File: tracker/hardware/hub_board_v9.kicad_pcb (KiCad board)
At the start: 4 copper layers, 103 x 103 mm, 39 parts, among them U1 ESP32-S3-WROOM-1U-N8R8, U2 LoRa2021F33-2G4, U3 LoRa2021_Castellated, U4 SX1280, U5 MAX-M10S, U6 MS5611-01BA, U7 TPS7A02

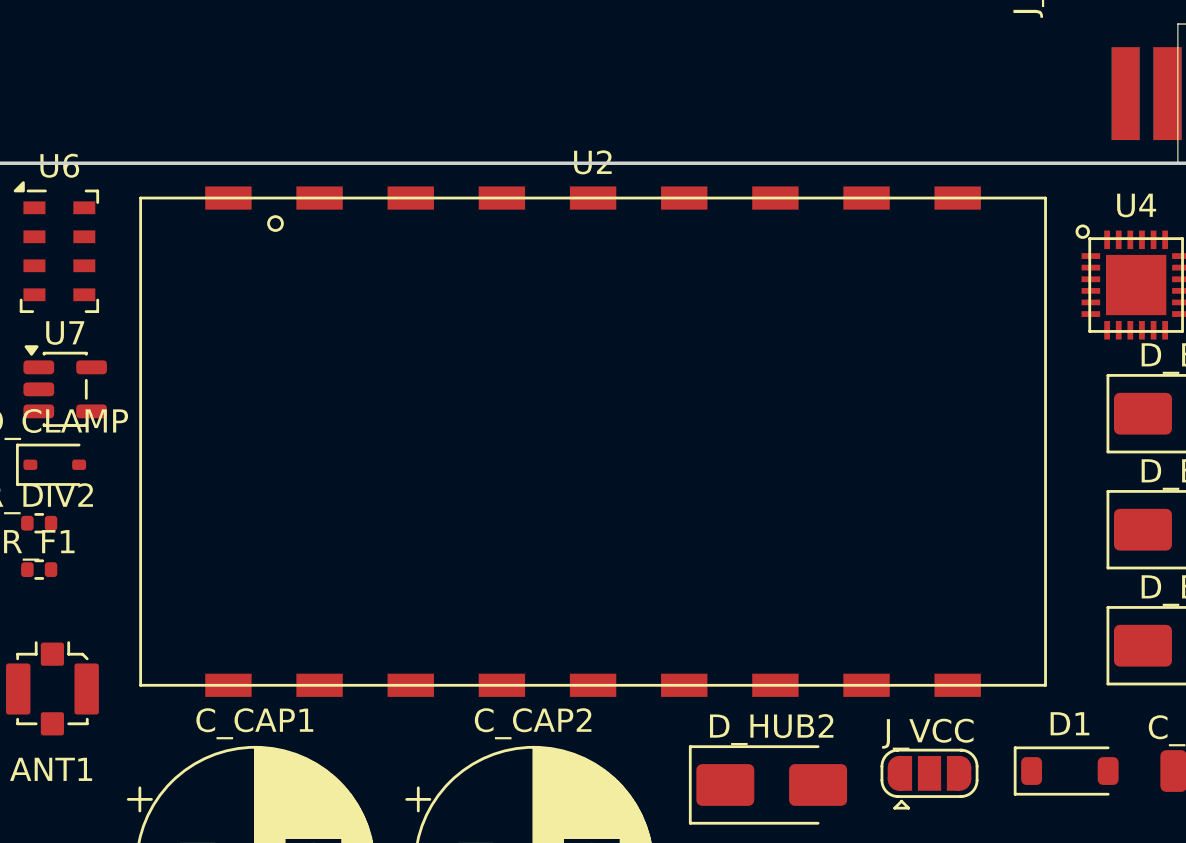
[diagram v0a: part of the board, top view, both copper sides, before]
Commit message: fix(hw/f33): derive the castellation land size from the operator-supplied 0.80mm datum
The F33 land pattern's pad POSITIONS were already verified against the vendor's own
Altium pad file; the pad SIZE was the one declared guess (2.0 x 1.0 mm, TODO(unverified)).
The operator read the vendor drawing (datasheet s9 "Mechanism Dimension" p8, an embedded
JPEG raster with no text layer, hence never extractable in-repo) and reported the
castellation hole diameter D = 0.80 +/- 0.10 mm.  That is the authoritative datum.

DERIVE the land instead of hard-coding it:
  rule: land = the castellation aperture grown by a uniform 0.25mm solder-fillet margin
        on every side.
    x (along the edge): D + 2*0.25 = 1.30mm  (was 2.0mm = 2.5xD);
                        gap to the next land = 3.9289 - 1.30 = 2.6289mm
    y (across the edge): D + 2*0.25 = 1.30mm, symmetric about the pad centre, which the
                        vendor file pins on the module edge and which must NOT move:
                          inward 0.65mm >= D/2 = 0.40mm
                          outward 0.65mm >= inward 0.65mm -- the hand-solder iron's
                          access is the design driver (every joint on this vehicle is
                          hand-soldered); 0.65mm clears a 0.5mm chisel tip.

- scripts/gen_f33_landpattern.py: the hard-coded LAND_*_MM constants are replaced by the
  derivation (CASTELLATION_D_MM, CASTELLATION_D_TOL_MM, LAND_FILLET_MARGIN_MM); the rule
  and arithmetic are in the docstring; the datum and its +/-0.1 tolerance are recorded;
  --land-length/--land-width are kept as explicit overrides; the TODO(unverified)
  land-size flag is DROPPED (no other TODO touched).
- All four committed footprint copies and the v9 design-of-record footprint regenerated.
  Pad POSITIONS unchanged: the 18 pad-centre list is byte-identical (sha256 960877b2...)
  before and after, the bbox is still 31.4312 x 21.0000mm, and only the pad-size histogram
  moves 2x1 -> 1.3x1.3.  --verify-all exits 0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
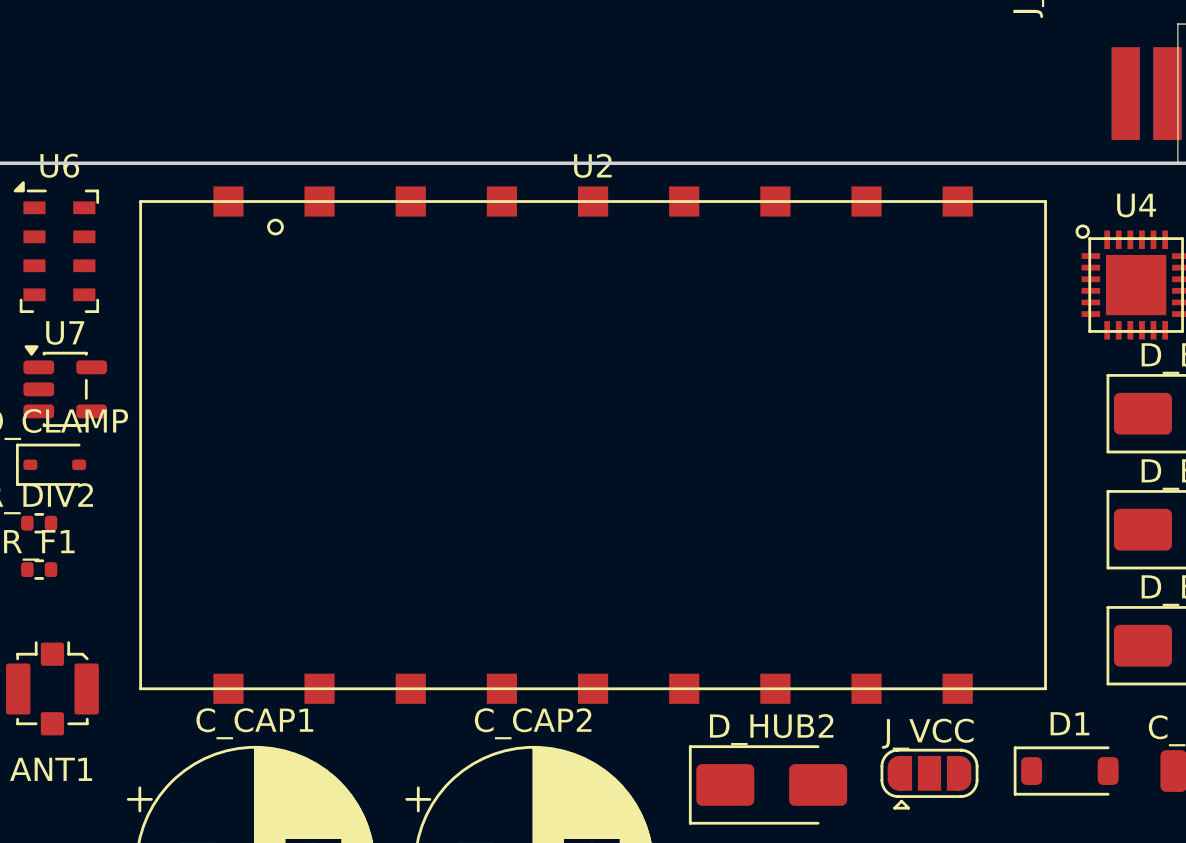
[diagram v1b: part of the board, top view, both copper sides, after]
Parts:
- moved U2 0.15 mm to (25.8, 12.2)
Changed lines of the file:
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@@
 	(footprint "balloon_flight_v9:LoRa2021F33_2G4"
 		(layer "F.Cu")
-		(at 25.845 12)
-		(descr "NiceRF LoRa2021F33-2G4, 18-pin castellated module (LR2021 + 2W PA + TCXO), 39x21mm. Pad CENTRES decoded from the vendor land file LORA2021F33-2G4 footprint_pads.pcb (pitch 3.9289mm, 9 pads on each 39mm edge). Land size 2.0x1.0 mm TODO(unverified): datasheet s9 p8 is a raster with no text layer.")
+		(at 25.845 12.15)
+		(descr "NiceRF LoRa2021F33-2G4, 18-pin castellated module (LR2021 + 2W PA + TCXO), 39x21mm. Pad CENTRES decoded from the vendor land file LORA2021F33-2G4 footprint_pads.pcb (pitch 3.9289mm, 9 pads on each 39mm edge). Land size 1.3 x 1.3 mm DERIVED from the operator-supplied castellation hole diameter D = 0.8 +/- 0.1 mm grown by a uniform 0.25 mm solder-fillet margin on every side (datasheet s9 p8, read by the operator 2026-10-07).")
 		(tags "LoRa LR2021 NiceRF F33 castellated PA 2W vendor-land-pattern")
 		(property "Reference" "U2"
@@
 		(pad "1" smd rect
 			(at -11.7867 -10.5)
-			(size 2 1)
+			(size 1.3 1.3)
 			(layers "F.Cu" "F.Mask" "F.Paste")
 			(net 17 "/F33_VCC")
@@
 		(pad "2" smd rect
 			(at -7.8578 -10.5)
-			(size 2 1)
+			(size 1.3 1.3)
 			(layers "F.Cu" "F.Mask" "F.Paste")
 			(net 51 "GND")
@@
 		(pad "3" smd rect
 			(at -3.9289 -10.5)
-			(size 2 1)
+			(size 1.3 1.3)
 			(layers "F.Cu" "F.Mask" "F.Paste")
 			(net 51 "GND")
@@
 		(pad "4" smd rect
 			(at 0 -10.5)
-			(size 2 1)
+			(size 1.3 1.3)
 			(layers "F.Cu" "F.Mask" "F.Paste")
 			(net 51 "GND")
@@
 		(pad "5" smd rect
 			(at 3.9289 -10.5)
-			(size 2 1)
+			(size 1.3 1.3)
 			(layers "F.Cu" "F.Mask" "F.Paste")
 			(net 1 "+3V3")
@@
 		(pad "6" smd rect
 			(at 7.8578 -10.5)
-			(size 2 1)
+			(size 1.3 1.3)
 			(layers "F.Cu" "F.Mask" "F.Paste")
 			(net 51 "GND")
@@
 		(pad "7" smd rect
 			(at 11.7867 -10.5)
-			(size 2 1)
+			(size 1.3 1.3)
 			(layers "F.Cu" "F.Mask" "F.Paste")
 			(net 51 "GND")
@@
 		(pad "8" smd rect
 			(at 15.7156 -10.5)
-			(size 2 1)
+			(size 1.3 1.3)
 			(layers "F.Cu" "F.Mask" "F.Paste")
 			(net 51 "GND")
@@
 		(pad "9" smd rect
 			(at 15.7156 10.5)
-			(size 2 1)
+			(size 1.3 1.3)
 			(layers "F.Cu" "F.Mask" "F.Paste")
 			(net 2 "/ANT1_433_TX")
@@
 		(pad "10" smd rect
 			(at 11.7867 10.5)
-			(size 2 1)
+			(size 1.3 1.3)
 			(layers "F.Cu" "F.Mask" "F.Paste")
 		)
 		(pad "11" smd rect
 			(at 7.8578 10.5)
-			(size 2 1)
+			(size 1.3 1.3)
 			(layers "F.Cu" "F.Mask" "F.Paste")
 			(net 51 "GND")
@@
 		(pad "12" smd rect
 			(at 3.9289 10.5)
-			(size 2 1)
+			(size 1.3 1.3)
 			(layers "F.Cu" "F.Mask" "F.Paste")
 			(net 16 "/F33_SCK")
@@
 		(pad "13" smd rect
 			(at 0 10.5)
-			(size 2 1)
+			(size 1.3 1.3)
 			(layers "F.Cu" "F.Mask" "F.Paste")
 			(net 11 "/F33_CS_N")
@@
 		(pad "14" smd rect
 			(at -3.9289 10.5)
-			(size 2 1)
+			(size 1.3 1.3)
 			(layers "F.Cu" "F.Mask" "F.Paste")
 			(net 10 "/F33_BUSY")
@@
 		(pad "15" smd rect
 			(at -7.8578 10.5)
-			(size 2 1)
+			(size 1.3 1.3)
 			(layers "F.Cu" "F.Mask" "F.Paste")
 			(net 14 "/F33_MOSI")
@@
 		(pad "16" smd rect
 			(at -11.7867 10.5)
-			(size 2 1)
+			(size 1.3 1.3)
 			(layers "F.Cu" "F.Mask" "F.Paste")
 			(net 13 "/F33_MISO")
@@
 		(pad "17" smd rect
 			(at -15.7156 10.5)
-			(size 2 1)
+			(size 1.3 1.3)
 			(layers "F.Cu" "F.Mask" "F.Paste")
 			(net 15 "/F33_RESET_N")
@@
 		(pad "18" smd rect
 			(at -15.7156 -10.5)
-			(size 2 1)
+			(size 1.3 1.3)
 			(layers "F.Cu" "F.Mask" "F.Paste")
 			(net 12 "/F33_IRQ")

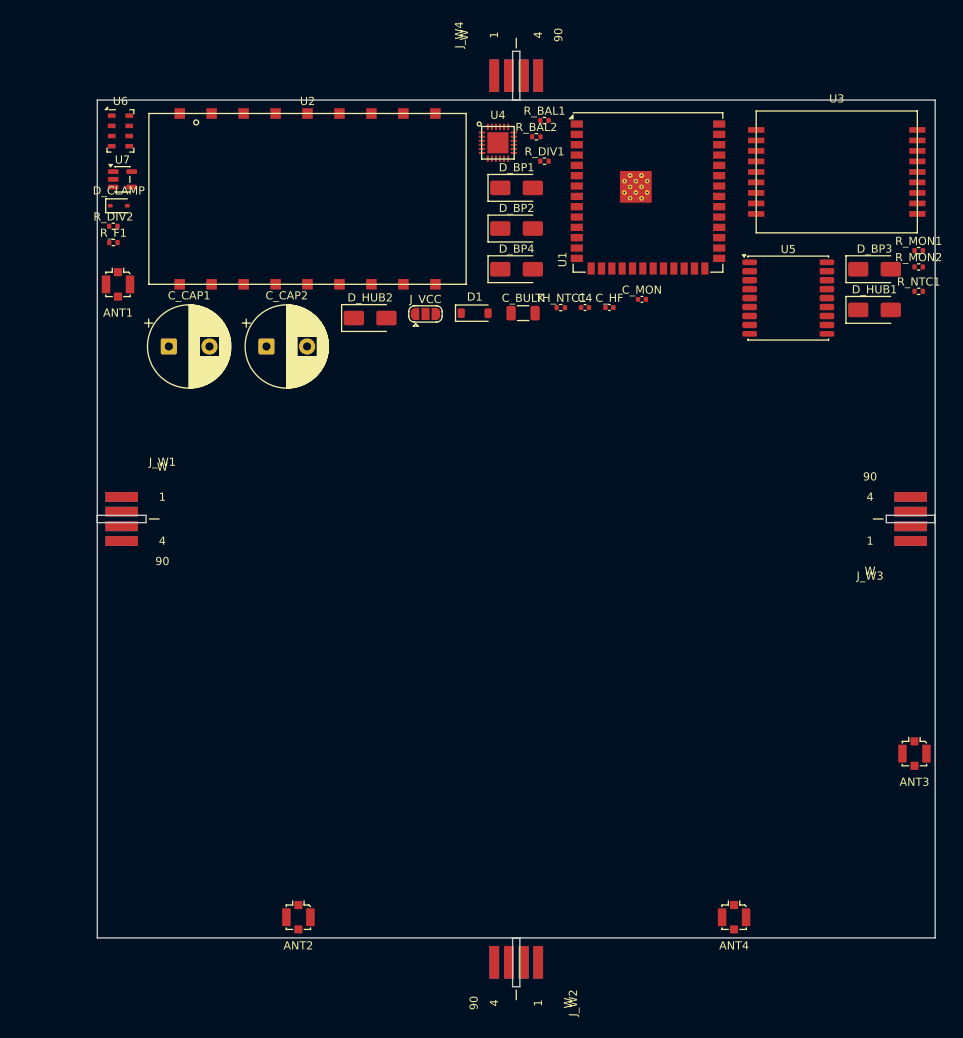
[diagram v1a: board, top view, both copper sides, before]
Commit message: fix(hw/hub): render fidelity — cells on the sun-facing face, faceted dark cells, no box parts
Recovered from a worker that timed out at 3600 s having completed the work but
not committed it. The generator died ONE LINE from publishing on:

    NameError: name 'KICAD9_3DMODEL_DIR' is not defined

because `${KICAD9_3DMODEL_DIR}` is a KiCad VARIABLE, not a Python name: inside
an f-string it parses as the expression KICAD9_3DMODEL_DIR. The module already
had a KICAD9_VAR constant for exactly this; the print did not use it. Fixed.

Three render defects, all verified after regeneration:

1. CELLS ON THE WRONG FACE (operator-reported, ADR-055 D6).
   PVA1/PVA2 were on B.Cu; every other footprint is F.Cu. ADR-055 D6 says the
   hub cells go on the UPPER/sun-facing face, and with a horizontal hub the
   downward face receives no direct sun. Now F.Cu.

2. CELLS RENDERED AS FLAT GREY SLABS (operator-reported).
   The hub cell model was a bare `Box` with ONE material (light grey), while the
   wing's was an `IndexedFaceSet` with TWO (dark cell face + light frame). That
   is why the wing's panels read as cells and the hub's as slabs. Now faceted
   with the dark 0.09 0.1 0.42 cell face, matching the wing.

3. IMPLAUSIBLY THICK PARTS (operator-reported).
   See the coverage report for every model's Z and its source.

Model split after regeneration: 25 library + 16 repo-local, unmapped: [].
Library models are referenced via ${KICAD9_3DMODEL_DIR}, so a render now
REQUIRES: export KICAD9_3DMODEL_DIR=/usr/share/kicad/3dmodels

Board sha256 1d4e9509e9528f5b5b696f7a52b644518c5bc5070fe633526a0085ee2df7f259
Full-duty check still reports honestly: 4 x LARGE = 122.2 cm2 > plate 106.09 cm2,
so the 4-cell 106.1 cm2 configuration is NOT placeable on a 103 x 103 mm plate
(the packing problem the operator's overhang decision resolves).
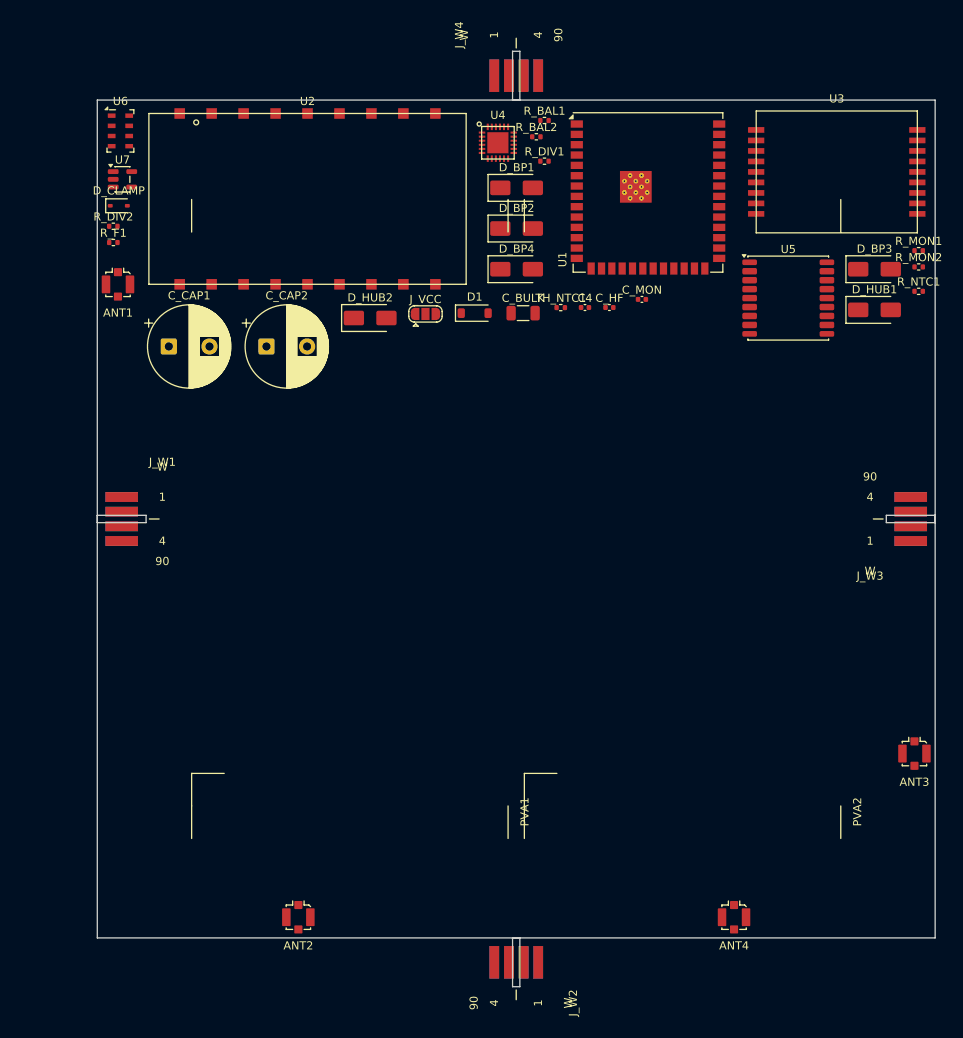
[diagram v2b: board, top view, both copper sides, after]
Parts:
- added PVA1: SolarCell_78x39mm, Array_Cells:SolarCell_LARGE_78x39mm, F.Cu at (31.1, 51.5)
- added PVA2: SolarCell_78x39mm, Array_Cells:SolarCell_LARGE_78x39mm, F.Cu at (72.0, 51.5)

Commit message: feat(hw/hub): implement ADR-063 overhanging solar carrier
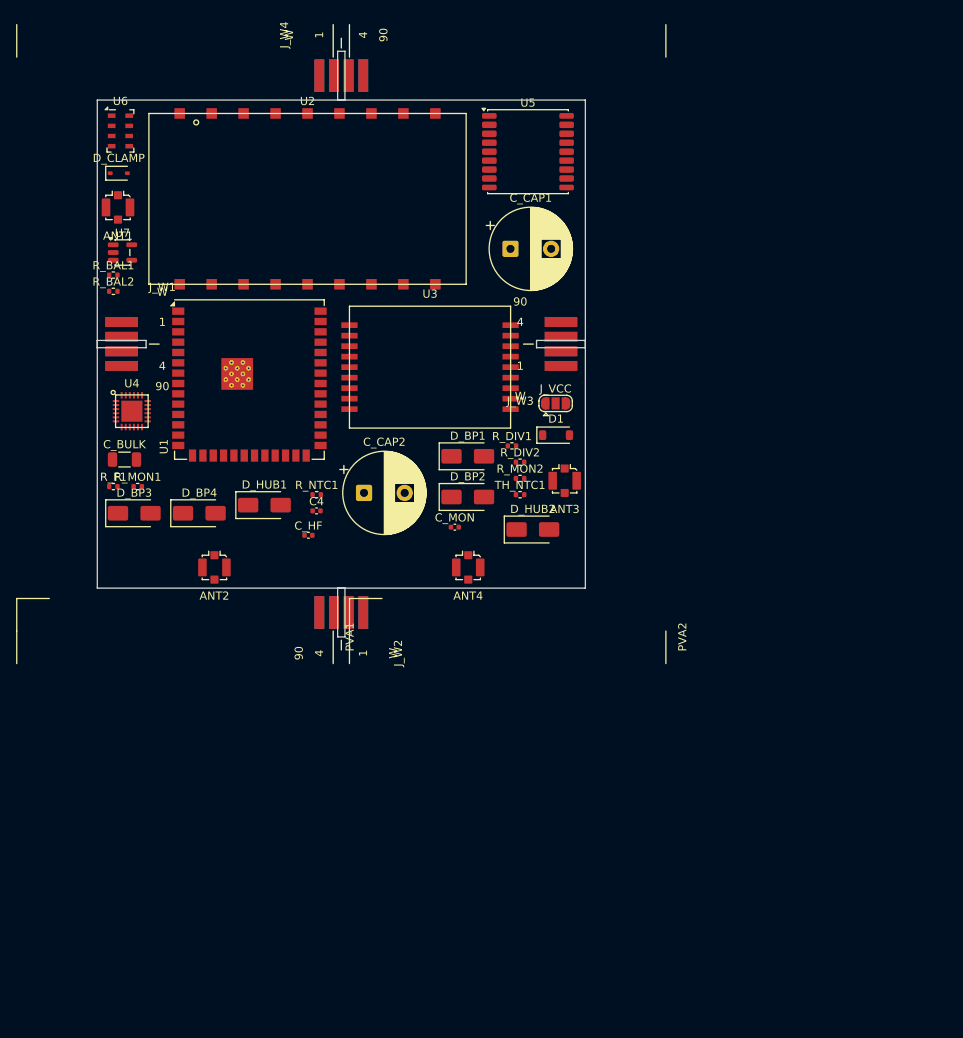
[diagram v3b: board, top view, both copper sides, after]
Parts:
- moved R_MON1 100.3 mm to (4.97, 47.5)
- moved D_BP3 95.8 mm to (4.54, 50.8)
- moved D_HUB1 78.7 mm to (20.5, 49.8)
- moved R_NTC1 78.1 mm to (27.0, 48.5)
- moved R_DIV2 57.8 mm to (52.0, 44.5)
- moved R_BAL1 56.3 mm to (1.98, 21.5)
- moved U4 55.8 mm to (4.25, 38.2)
- moved R_MON2 55.5 mm to (52.0, 46.5)
- moved U3 55.5 mm to (40.9, 32.8)
- moved R_BAL2 55.4 mm to (1.98, 23.5)
- moved ANT3 54.5 mm to (57.5, 46.8)
- moved U1 54.1 mm to (18.7, 34.4)
- moved ANT4 54.0 mm to (45.6, 57.5)
- moved C_BULK 52.2 mm to (3.35, 44.2)
- moved D_BP4 49.2 mm to (12.5, 50.8)
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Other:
- board size 103 x 103 mm -> 60 x 60 mm
